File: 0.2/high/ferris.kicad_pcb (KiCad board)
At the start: 2 copper layers, 219.1 x 95.2 mm, 109 parts, among them J1 TYPE-C-31-M-12, K0_0 KEYSW, K0_1 KEYSW, K0_2 KEYSW, K0_3 KEYSW, K0_4 KEYSW, K0_5 KEYSW, K0_6 KEYSW, K0_7 KEYSW, K0_8 KEYSW, K0_9 KEYSW, K1_0 KEYSW, K1_1 KEYSW, K1_2 KEYSW, K1_3 KEYSW, K1_4 KEYSW, K1_5 KEYSW, K1_6 KEYSW, K1_7 KEYSW, K1_8 KEYSW, K1_9 KEYSW, K2_0 KEYSW, K2_1 KEYSW, K2_2 KEYSW, K2_3 KEYSW, K2_4 KEYSW, K2_5 KEYSW, K2_6 KEYSW, K2_7 KEYSW, K2_8 KEYSW, K2_9 KEYSW, K3_3 KEYSW, K3_4 KEYSW, K3_5 KEYSW, K3_6 KEYSW, Q1 PDTC123JT,215, SW1 B3U-1000P, U1 STM32F072CBT6, U2 MCP23017-E/SO, U3 MCP1700T-3302E/TT, U4 SRV05-4

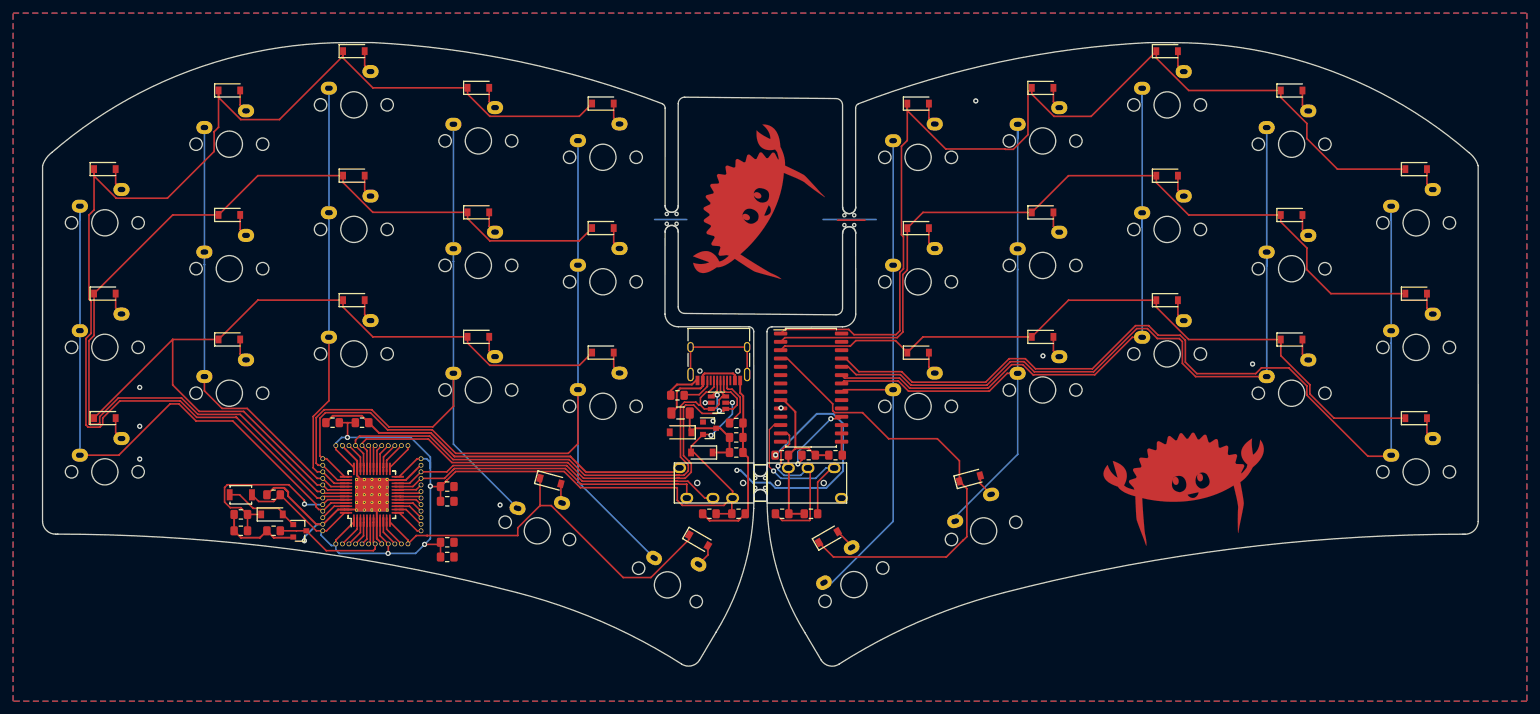
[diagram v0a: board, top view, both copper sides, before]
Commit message: Update to KiCad 7.0
... and prune outdated project files (need to check)
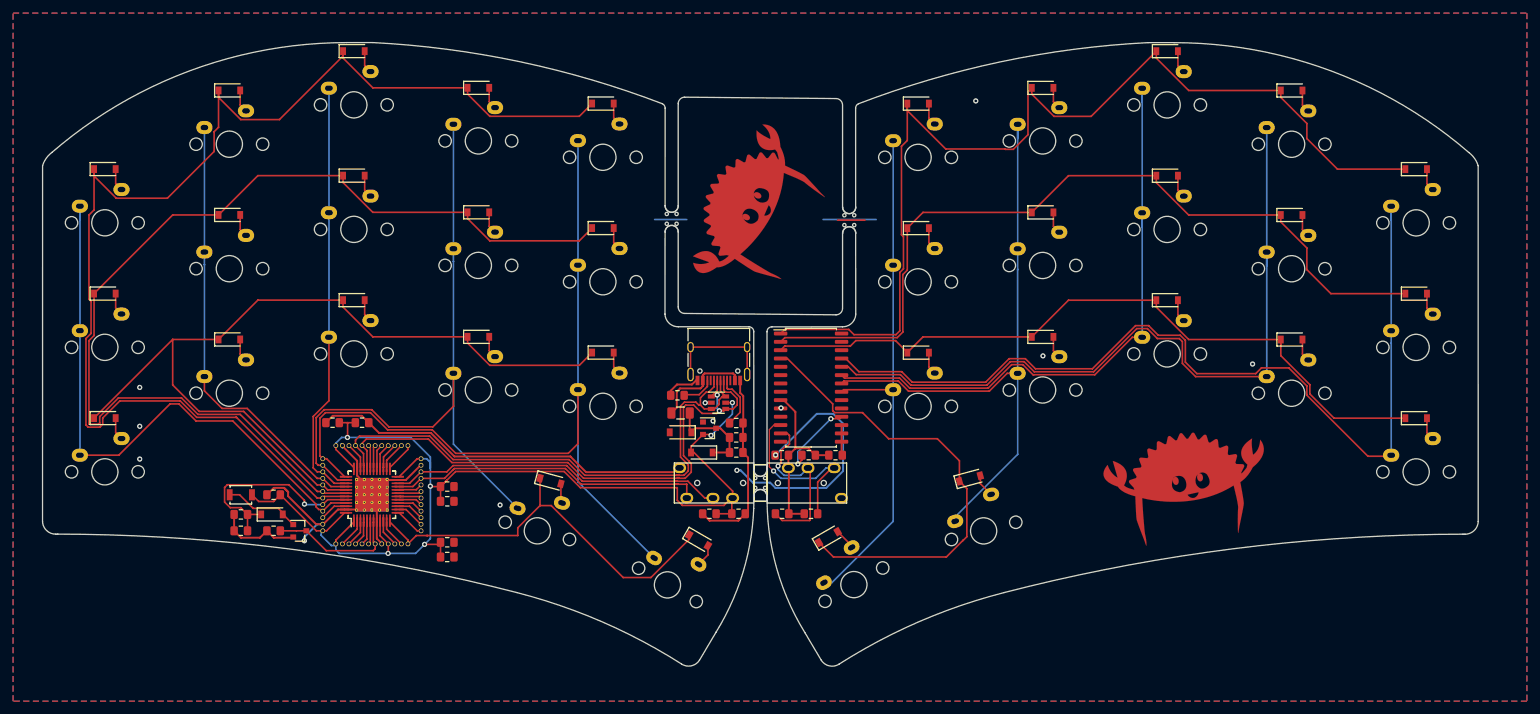
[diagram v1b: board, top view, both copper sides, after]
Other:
- net class Default removed
- net class Power removed

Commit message: Begin attempting to fix schematic bug
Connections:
- J1 pad A8: Net-(J1-PadA8) -> unconnected-(J1-SBU1-PadA8)
- J1 pad B8: Net-(J1-PadB8) -> unconnected-(J1-SBU2-PadB8)
- J1 pad S1: Net-(J1-PadS1) -> unconnected-(J1-SHIELD-PadS1)
- U1 pad 10: Net-(U1-Pad10) -> unconnected-(U1-PA0-Pad10)
- U1 pad 11: Net-(U1-Pad11) -> unconnected-(U1-PA1-Pad11)
- U1 pad 13: Net-(U1-Pad13) -> unconnected-(U1-PA3-Pad13)
- U1 pad 14: Net-(U1-Pad14) -> unconnected-(U1-PA4-Pad14)
- U1 pad 15: Net-(U1-Pad15) -> unconnected-(U1-PA5-Pad15)
- U1 pad 16: Net-(U1-Pad16) -> unconnected-(U1-PA6-Pad16)
- U1 pad 17: Net-(U1-Pad17) -> unconnected-(U1-PA7-Pad17)
- U1 pad 18: Net-(U1-Pad18) -> unconnected-(U1-PB0-Pad18)
- U1 pad 19: Net-(U1-Pad19) -> unconnected-(U1-PB1-Pad19)
- U1 pad 2: Net-(U1-Pad2) -> unconnected-(U1-PC13-Pad2)
- U1 pad 20: Net-(U1-Pad20) -> unconnected-(U1-PB2-Pad20)
- U1 pad 25: Net-(U1-Pad25) -> unconnected-(U1-PB12-Pad25)
- U1 pad 26: Net-(U1-Pad26) -> unconnected-(U1-PB13-Pad26)
- U1 pad 27: Net-(U1-Pad27) -> unconnected-(U1-PB14-Pad27)
- U1 pad 28: Net-(U1-Pad28) -> unconnected-(U1-PB15-Pad28)
- U1 pad 29: Net-(U1-Pad29) -> unconnected-(U1-PA8-Pad29)
- U1 pad 3: Net-(U1-Pad3) -> unconnected-(U1-PC14-Pad3)
- U1 pad 30: Net-(U1-Pad30) -> unconnected-(U1-PA9-Pad30)
- U1 pad 31: Net-(U1-Pad31) -> unconnected-(U1-PA10-Pad31)
- U1 pad 34: Net-(U1-Pad34) -> unconnected-(U1-PA13-Pad34)
- U1 pad 4: Net-(U1-Pad4) -> unconnected-(U1-PC15-Pad4)
- U1 pad 46: Net-(U1-Pad46) -> unconnected-(U1-PB9-Pad46)
- U1 pad 5: Net-(U1-Pad5) -> unconnected-(U1-PF0-Pad5)
- U1 pad 6: Net-(U1-Pad6) -> unconnected-(U1-PF1-Pad6)
- U2 pad 11: Net-(U2-Pad11) -> unconnected-(U2-NC-Pad11)
- U2 pad 14: Net-(U2-Pad14) -> unconnected-(U2-NC-Pad14)
- U2 pad 19: Net-(U2-Pad19) -> unconnected-(U2-INTB-Pad19)
- U2 pad 20: Net-(U2-Pad20) -> unconnected-(U2-INTA-Pad20)
- U2 pad 26: Net-(U2-Pad26) -> unconnected-(U2-GPA5-Pad26)
- U2 pad 27: Net-(U2-Pad27) -> unconnected-(U2-GPA6-Pad27)
- U2 pad 28: Net-(U2-Pad28) -> unconnected-(U2-GPA7-Pad28)
- U2 pad 5: Net-(U2-Pad5) -> unconnected-(U2-GPB4-Pad5)
- U2 pad 6: Net-(U2-Pad6) -> unconnected-(U2-GPB5-Pad6)
- U2 pad 7: Net-(U2-Pad7) -> unconnected-(U2-GPB6-Pad7)
- U2 pad 8: Net-(U2-Pad8) -> unconnected-(U2-GPB7-Pad8)
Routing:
- net unconnected-(J1-SHIELD-PadS1): track 0.00 -> 17.0 mm
- net Net-(J1-PadS1): track 17.0 -> 0.00 mm
- net unconnected-(U1-PA0-Pad10): track 0.00 -> 4.79 mm
- net Net-(U1-Pad10): track 4.79 -> 0.00 mm
- net unconnected-(U1-PB12-Pad25): track 0.00 -> 4.48 mm
- net unconnected-(U1-PA3-Pad13): track 0.00 -> 4.48 mm
- net Net-(U1-Pad25): track 4.48 -> 0.00 mm
- net Net-(U1-Pad13): track 4.48 -> 0.00 mm
- net unconnected-(U1-PC13-Pad2): track 0.00 -> 4.27 mm
- net unconnected-(U1-PB13-Pad26): track 0.00 -> 4.27 mm
- net unconnected-(U1-PA4-Pad14): track 0.00 -> 4.27 mm
- net unconnected-(U1-PA1-Pad11): track 0.00 -> 4.27 mm
- net Net-(U1-Pad26): track 4.27 -> 0.00 mm
- net Net-(U1-Pad2): track 4.27 -> 0.00 mm
- net Net-(U1-Pad14): track 4.27 -> 0.00 mm
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
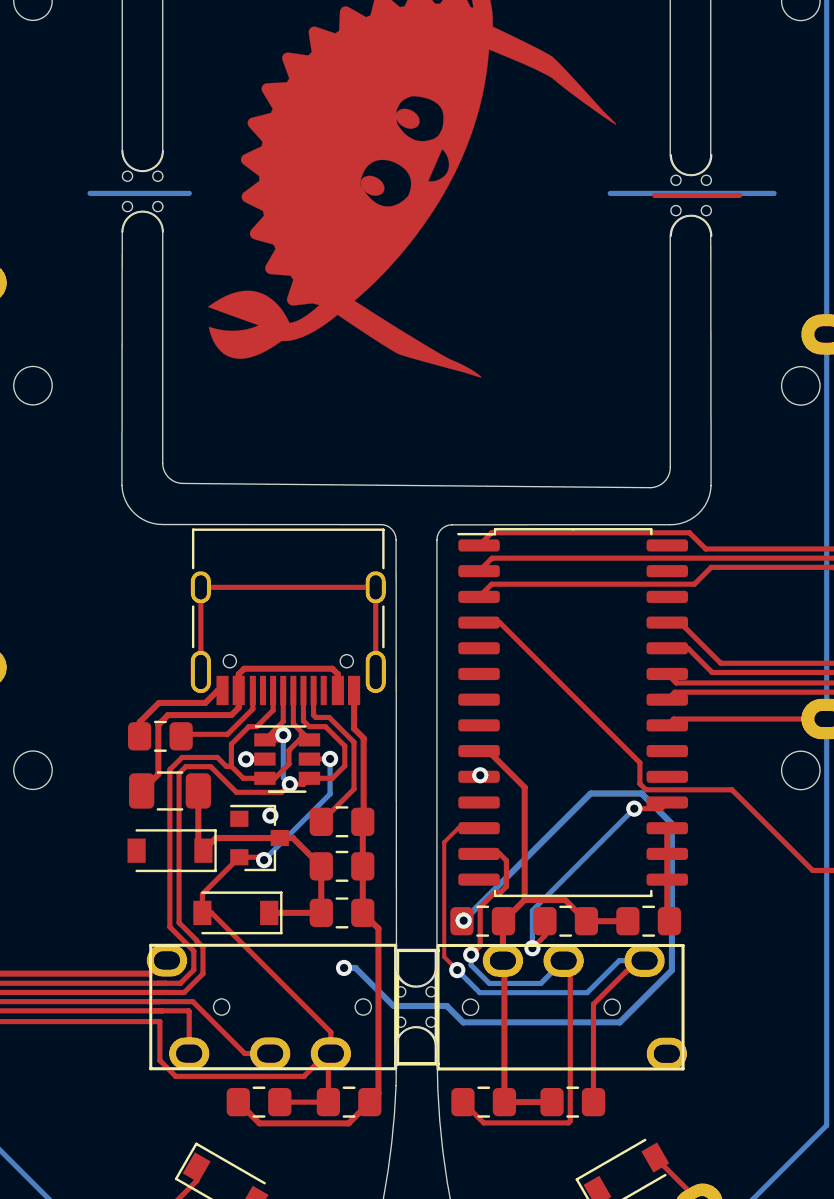
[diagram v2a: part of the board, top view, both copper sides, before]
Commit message: Attempt to replicate df923a93 Make all mouse bites 5mm
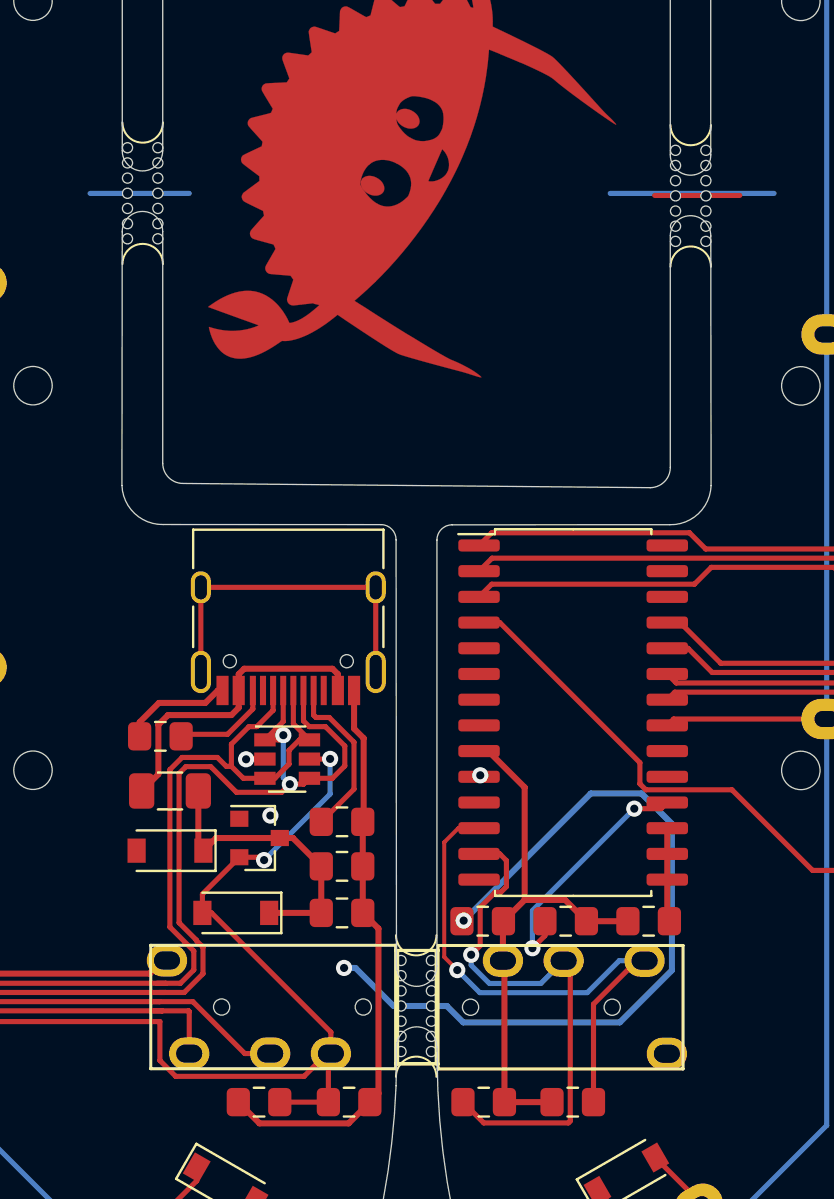
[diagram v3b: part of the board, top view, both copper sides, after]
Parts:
- REF** (x3): value mouse-bite-2mm-slot-with-space-for-track -> VAL**; footprint panelization:mouse-bite-2mm-slot-with-space-for-track -> panelization:mouse-bite-5mm-slot
- moved REF** 1.59 mm to (110.5, 43.0)
- moved REF** 1.52 mm to (137.6, 43.1)
- moved REF** 1.45 mm to (124.0, 83.2)
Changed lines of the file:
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@@
       (stroke (width 0.01) (type solid)) (fill solid) (layer "F.Mask"))
   )
-  (footprint "panelization:mouse-bite-2mm-slot-with-space-for-track" locked (layer "F.Cu")
-    (at 137.6 41.6 90)
-    (attr exclude_from_pos_files exclude_from_bom)
-    (fp_text reference "REF**" (at 0 0 90) (layer "F.SilkS") hide
-        (effects (font (size 1 1) (thickness 0.15)))
+  (footprint "panelization:mouse-bite-5mm-slot" locked (layer "F.Cu")
+    (at 137.5784 43.12 90)
+    (attr through_hole)
+    (fp_text reference "REF**" (at 0 -2 90) (layer "F.SilkS") hide
+        (effects (font (size 1 1) (thickness 0.2)))
     )
-    (fp_text value "mouse-bite-2mm-slot-with-space-for-track" (at 0 2 90) (layer "F.Fab") hide
-        (effects (font (size 1 1) (thickness 0.15)))
+    (fp_text value "VAL**" (at 0 2.1 90) (layer "F.SilkS") hide
+        (effects (font (size 1 1) (thickness 0.2)))
     )
     (fp_arc (start -2 -1) (mid -1 0) (end -2 1)
       (stroke (width 0.1) (type solid)) (layer "F.SilkS"))
-    (fp_arc (start 2 1) (mid 1 0) (end 2 -1)
+    (fp_arc (start 5 1) (mid 4 0) (end 5 -1)
       (stroke (width 0.1) (type solid)) (layer "F.SilkS"))
     (fp_circle (center -2 0) (end -2 -0.06)
       (stroke (width 0.05) (type solid)) (fill none) (layer "Dwgs.User"))
-    (fp_circle (center 2 0) (end 2.06 0)
+    (fp_circle (center 5 0) (end 5.06 0)
       (stroke (width 0.05) (type solid)) (fill none) (layer "Dwgs.User"))
     (fp_line (start -2 0) (end -2 0)
       (stroke (width 2) (type solid)) (layer "Eco1.User"))
-    (fp_line (start 2 0) (end 2 0)
+    (fp_line (start 5 0) (end 5 0)
       (stroke (width 2) (type solid)) (layer "Eco1.User"))
     (pad "" np_thru_hole circle locked (at -0.75 -0.75 90) (size 0.5 0.5) (drill 0.5) (layers "*.Cu" "*.Mask"))
     (pad "" np_thru_hole circle locked (at -0.75 0.75 90) (size 0.5 0.5) (drill 0.5) (layers "*.Cu" "*.Mask"))
+    (pad "" np_thru_hole circle locked (at 0 -0.75 90) (size 0.5 0.5) (drill 0.5) (layers "*.Cu" "*.Mask"))
+    (pad "" np_thru_hole circle locked (at 0 0.75 90) (size 0.5 0.5) (drill 0.5) (layers "*.Cu" "*.Mask"))
     (pad "" np_thru_hole circle locked (at 0.75 -0.75 90) (size 0.5 0.5) (drill 0.5) (layers "*.Cu" "*.Mask"))
     (pad "" np_thru_hole circle locked (at 0.75 0.75 90) (size 0.5 0.5) (drill 0.5) (layers "*.Cu" "*.Mask"))
+    (pad "" np_thru_hole circle locked (at 1.5 -0.75 90) (size 0.5 0.5) (drill 0.5) (layers "*.Cu" "*.Mask"))
+    (pad "" np_thru_hole circle locked (at 1.5 0.75 90) (size 0.5 0.5) (drill 0.5) (layers "*.Cu" "*.Mask"))
+    (pad "" np_thru_hole circle locked (at 2.25 -0.75 90) (size 0.5 0.5) (drill 0.5) (layers "*.Cu" "*.Mask"))
+    (pad "" np_thru_hole circle locked (at 2.25 0.75 90) (size 0.5 0.5) (drill 0.5) (layers "*.Cu" "*.Mask"))
+    (pad "" np_thru_hole circle locked (at 3 -0.75 90) (size 0.5 0.5) (drill 0.5) (layers "*.Cu" "*.Mask"))
+    (pad "" np_thru_hole circle locked (at 3 0.75 90) (size 0.5 0.5) (drill 0.5) (layers "*.Cu" "*.Mask"))
+    (pad "" np_thru_hole circle locked (at 3.75 -0.75 90) (size 0.5 0.5) (drill 0.5) (layers "*.Cu" "*.Mask"))
+    (pad "" np_thru_hole circle locked (at 3.75 0.75 90) (size 0.5 0.5) (drill 0.5) (layers "*.Cu" "*.Mask"))
   )
-  (footprint "panelization:mouse-bite-2mm-slot-with-space-for-track" locked (layer "F.Cu")
-    (at 124 81.7 90)
-    (attr exclude_from_pos_files exclude_from_bom)
-    (fp_text reference "REF**" (at 0 0 90) (layer "F.SilkS") hide
-        (effects (font (size 1 1) (thickness 0.15)))
+  (footprint "panelization:mouse-bite-5mm-slot" locked (layer "F.Cu")
+    (at 124.0148 83.1504 90)
+    (attr through_hole)
+    (fp_text reference "REF**" (at 0 -2 90) (layer "F.SilkS") hide
+        (effects (font (size 1 1) (thickness 0.2)))
     )
-    (fp_text value "mouse-bite-2mm-slot-with-space-for-track" (at 0 2 90) (layer "F.Fab") hide
-        (effects (font (size 1 1) (thickness 0.15)))
+    (fp_text value "VAL**" (at 0 2.1 90) (layer "F.SilkS") hide
+        (effects (font (size 1 1) (thickness 0.2)))
     )
     (fp_arc (start -2 -1) (mid -1 0) (end -2 1)
       (stroke (width 0.1) (type solid)) (layer "F.SilkS"))
-    (fp_arc (start 2 1) (mid 1 0) (end 2 -1)
+    (fp_arc (start 5 1) (mid 4 0) (end 5 -1)
       (stroke (width 0.1) (type solid)) (layer "F.SilkS"))
     (fp_circle (center -2 0) (end -2 -0.06)
       (stroke (width 0.05) (type solid)) (fill none) (layer "Dwgs.User"))
-    (fp_circle (center 2 0) (end 2.06 0)
+    (fp_circle (center 5 0) (end 5.06 0)
       (stroke (width 0.05) (type solid)) (fill none) (layer "Dwgs.User"))
     (fp_line (start -2 0) (end -2 0)
       (stroke (width 2) (type solid)) (layer "Eco1.User"))
-    (fp_line (start 2 0) (end 2 0)
+    (fp_line (start 5 0) (end 5 0)
       (stroke (width 2) (type solid)) (layer "Eco1.User"))
     (pad "" np_thru_hole circle locked (at -0.75 -0.75 90) (size 0.5 0.5) (drill 0.5) (layers "*.Cu" "*.Mask"))
     (pad "" np_thru_hole circle locked (at -0.75 0.75 90) (size 0.5 0.5) (drill 0.5) (layers "*.Cu" "*.Mask"))
+    (pad "" np_thru_hole circle locked (at 0 -0.75 90) (size 0.5 0.5) (drill 0.5) (layers "*.Cu" "*.Mask"))
+    (pad "" np_thru_hole circle locked (at 0 0.75 90) (size 0.5 0.5) (drill 0.5) (layers "*.Cu" "*.Mask"))
     (pad "" np_thru_hole circle locked (at 0.75 -0.75 90) (size 0.5 0.5) (drill 0.5) (layers "*.Cu" "*.Mask"))
     (pad "" np_thru_hole circle locked (at 0.75 0.75 90) (size 0.5 0.5) (drill 0.5) (layers "*.Cu" "*.Mask"))
+    (pad "" np_thru_hole circle locked (at 1.5 -0.75 90) (size 0.5 0.5) (drill 0.5) (layers "*.Cu" "*.Mask"))
+    (pad "" np_thru_hole circle locked (at 1.5 0.75 90) (size 0.5 0.5) (drill 0.5) (layers "*.Cu" "*.Mask"))
+    (pad "" np_thru_hole circle locked (at 2.25 -0.75 90) (size 0.5 0.5) (drill 0.5) (layers "*.Cu" "*.Mask"))
+    (pad "" np_thru_hole circle locked (at 2.25 0.75 90) (size 0.5 0.5) (drill 0.5) (layers "*.Cu" "*.Mask"))
+    (pad "" np_thru_hole circle locked (at 3 -0.75 90) (size 0.5 0.5) (drill 0.5) (layers "*.Cu" "*.Mask"))
+    (pad "" np_thru_hole circle locked (at 3 0.75 90) (size 0.5 0.5) (drill 0.5) (layers "*.Cu" "*.Mask"))
+    (pad "" np_thru_hole circle locked (at 3.75 -0.75 90) (size 0.5 0.5) (drill 0.5) (layers "*.Cu" "*.Mask"))
+    (pad "" np_thru_hole circle locked (at 3.75 0.75 90) (size 0.5 0.5) (drill 0.5) (layers "*.Cu" "*.Mask"))
   )
-  (footprint "panelization:mouse-bite-2mm-slot-with-space-for-track" locked (layer "F.Cu")
-    (at 110.5 41.4 90)
-    (attr exclude_from_pos_files exclude_from_bom)
-    (fp_text reference "REF**" (at 0 0 90) (layer "F.SilkS") hide
-        (effects (font (size 1 1) (thickness 0.15)))
+  (footprint "panelization:mouse-bite-5mm-slot" locked (layer "F.Cu")
+    (at 110.5 42.993 90)
+    (attr through_hole)
+    (fp_text reference "REF**" (at 0 -2 90) (layer "F.SilkS") hide
+        (effects (font (size 1 1) (thickness 0.2)))
     )
-    (fp_text value "mouse-bite-2mm-slot-with-space-for-track" (at 0 2 90) (layer "F.Fab") hide
-        (effects (font (size 1 1) (thickness 0.15)))
+    (fp_text value "VAL**" (at 0 2.1 90) (layer "F.SilkS") hide
+        (effects (font (size 1 1) (thickness 0.2)))
     )
     (fp_arc (start -2 -1) (mid -1 0) (end -2 1)
       (stroke (width 0.1) (type solid)) (layer "F.SilkS"))
-    (fp_arc (start 2 1) (mid 1 0) (end 2 -1)
+    (fp_arc (start 5 1) (mid 4 0) (end 5 -1)
       (stroke (width 0.1) (type solid)) (layer "F.SilkS"))
     (fp_circle (center -2 0) (end -2 -0.06)
       (stroke (width 0.05) (type solid)) (fill none) (layer "Dwgs.User"))
-    (fp_circle (center 2 0) (end 2.06 0)
+    (fp_circle (center 5 0) (end 5.06 0)
       (stroke (width 0.05) (type solid)) (fill none) (layer "Dwgs.User"))
     (fp_line (start -2 0) (end -2 0)
       (stroke (width 2) (type solid)) (layer "Eco1.User"))
-    (fp_line (start 2 0) (end 2 0)
+    (fp_line (start 5 0) (end 5 0)
       (stroke (width 2) (type solid)) (layer "Eco1.User"))
     (pad "" np_thru_hole circle locked (at -0.75 -0.75 90) (size 0.5 0.5) (drill 0.5) (layers "*.Cu" "*.Mask"))
     (pad "" np_thru_hole circle locked (at -0.75 0.75 90) (size 0.5 0.5) (drill 0.5) (layers "*.Cu" "*.Mask"))
+    (pad "" np_thru_hole circle locked (at 0 -0.75 90) (size 0.5 0.5) (drill 0.5) (layers "*.Cu" "*.Mask"))
+    (pad "" np_thru_hole circle locked (at 0 0.75 90) (size 0.5 0.5) (drill 0.5) (layers "*.Cu" "*.Mask"))
     (pad "" np_thru_hole circle locked (at 0.75 -0.75 90) (size 0.5 0.5) (drill 0.5) (layers "*.Cu" "*.Mask"))
     (pad "" np_thru_hole circle locked (at 0.75 0.75 90) (size 0.5 0.5) (drill 0.5) (layers "*.Cu" "*.Mask"))
+    (pad "" np_thru_hole circle locked (at 1.5 -0.75 90) (size 0.5 0.5) (drill 0.5) (layers "*.Cu" "*.Mask"))
+    (pad "" np_thru_hole circle locked (at 1.5 0.75 90) (size 0.5 0.5) (drill 0.5) (layers "*.Cu" "*.Mask"))
+    (pad "" np_thru_hole circle locked (at 2.25 -0.75 90) (size 0.5 0.5) (drill 0.5) (layers "*.Cu" "*.Mask"))
+    (pad "" np_thru_hole circle locked (at 2.25 0.75 90) (size 0.5 0.5) (drill 0.5) (layers "*.Cu" "*.Mask"))
+    (pad "" np_thru_hole circle locked (at 3 -0.75 90) (size 0.5 0.5) (drill 0.5) (layers "*.Cu" "*.Mask"))
+    (pad "" np_thru_hole circle locked (at 3 0.75 90) (size 0.5 0.5) (drill 0.5) (layers "*.Cu" "*.Mask"))
+    (pad "" np_thru_hole circle locked (at 3.75 -0.75 90) (size 0.5 0.5) (drill 0.5) (layers "*.Cu" "*.Mask"))
+    (pad "" np_thru_hole circle locked (at 3.75 0.75 90) (size 0.5 0.5) (drill 0.5) (layers "*.Cu" "*.Mask"))
   )
   (footprint "silkscreens:safe_rust" locked (layer "B.Cu")
